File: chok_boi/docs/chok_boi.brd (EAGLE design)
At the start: 372 x 192 mm, 91 parts, among them U1 MPU-6000, U2 DRV8835

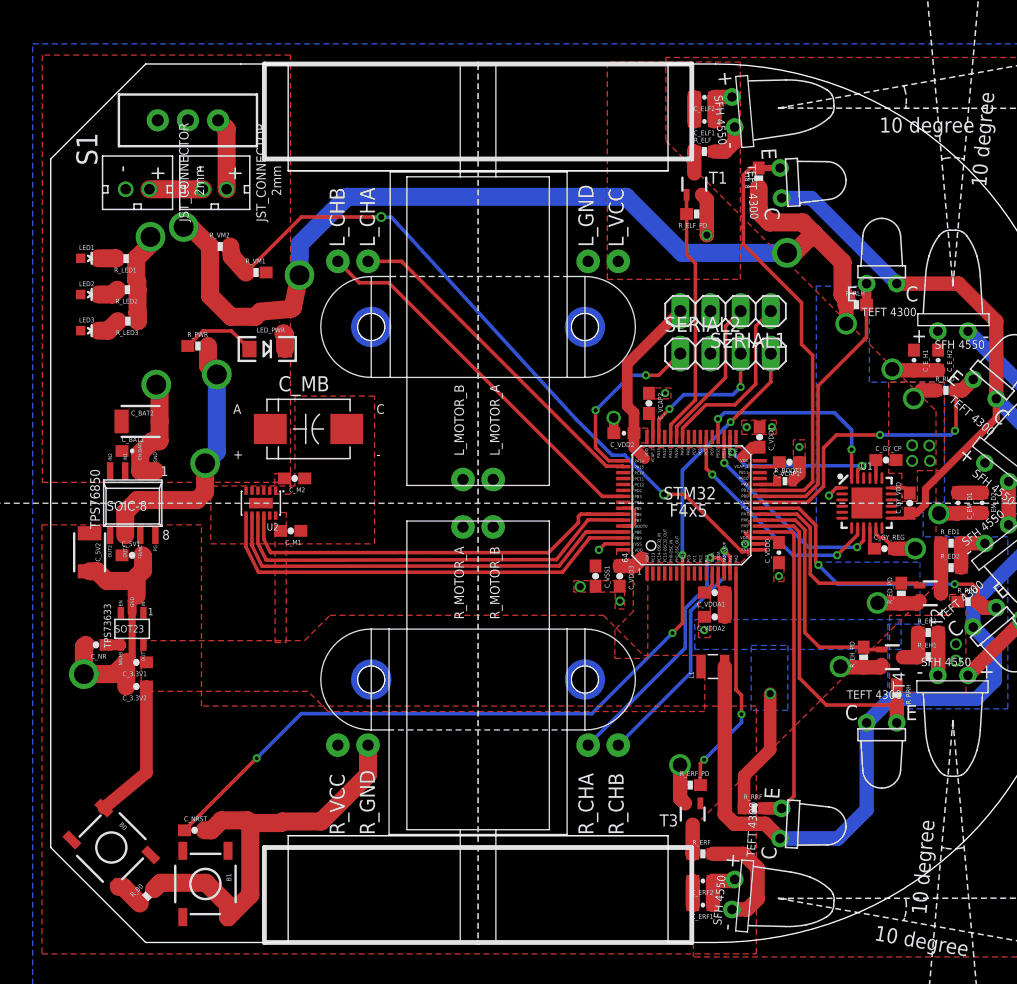
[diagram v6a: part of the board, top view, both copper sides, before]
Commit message: No more airwires!
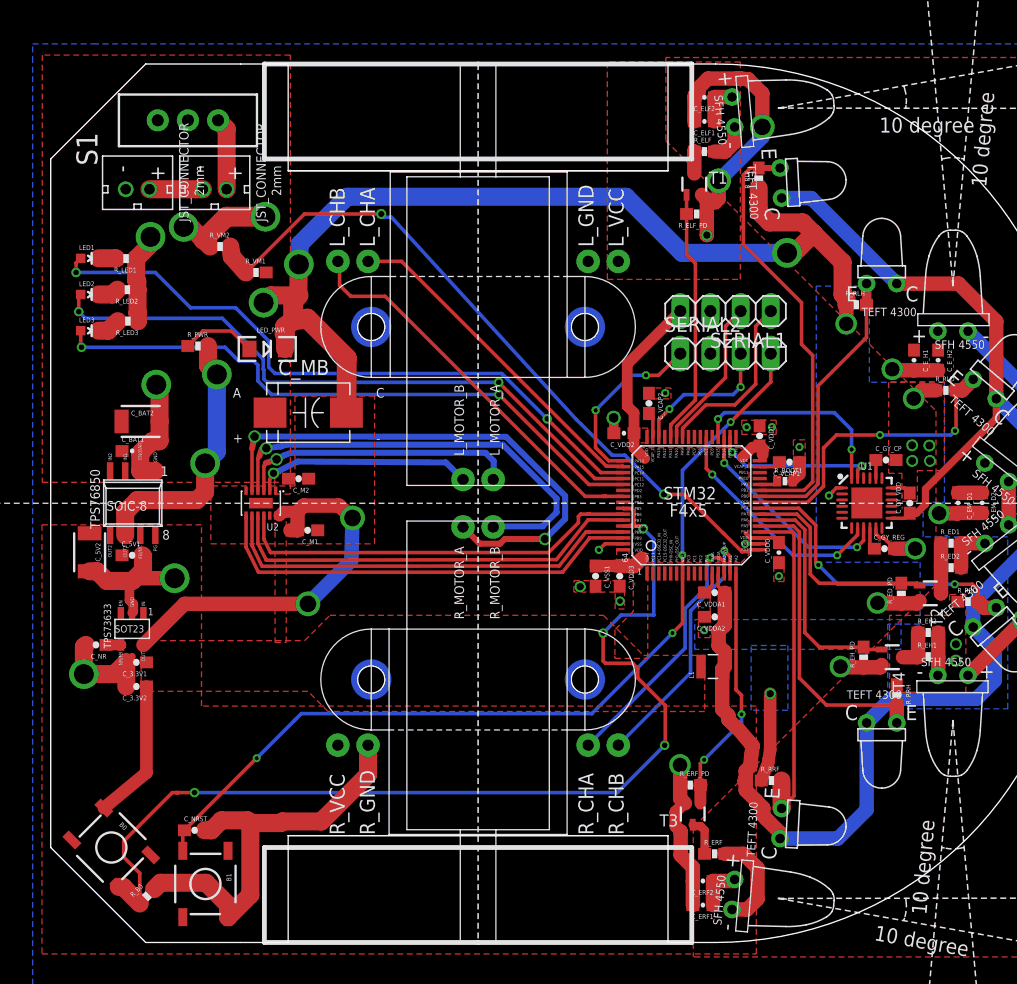
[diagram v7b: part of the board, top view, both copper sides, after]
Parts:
- moved R_RRF 2.75 mm to (60.7, 13.6)
- moved C_M1 1.42 mm to (21.6, 34.7)
- moved C_MB 1.37 mm to (21.7, 44.6)
- moved U$15 1.33 mm to (20.9, 54.5)
- moved U$16 1.15 mm to (20.4, 52.4)
- moved R_ERF 0.99 mm to (55.9, 7.47)
- moved C_M2 0.33 mm to (20.9, 39.1)
- moved C_VDD1 0.10 mm to (59.7, 42.7)
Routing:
- net BOOT0: track 5.49 -> 87.1 mm, vias 0 -> 4
- net LED1: track 0.00 -> 55.7 mm, vias 0 -> 2
- net LED2: track 0.00 -> 54.2 mm, vias 0 -> 2
- net LED3: track 0.00 -> 52.6 mm, vias 0 -> 2
- net MRF: track 0.00 -> 44.9 mm, vias 0 -> 2
- net MRB: track 0.00 -> 37.3 mm, vias 0 -> 1
- net 3.3V: track 33.9 -> 70.5 mm, vias 0 -> 2
- net GND: track 123.9 -> 151.3 mm, vias 20 -> 25
- net MLF: track 0.00 -> 23.6 mm, vias 0 -> 1
- net MLB: track 0.00 -> 18.3 mm, vias 0 -> 1
- net MGND: track 0.00 -> 10.5 mm
- net AGND: track 91.4 -> 86.9 mm
- net A3.3V: track 121.3 -> 125.0 mm
- net RESET: track 75.1 -> 76.9 mm
- net EM_RF: track 19.5 -> 21.0 mm
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
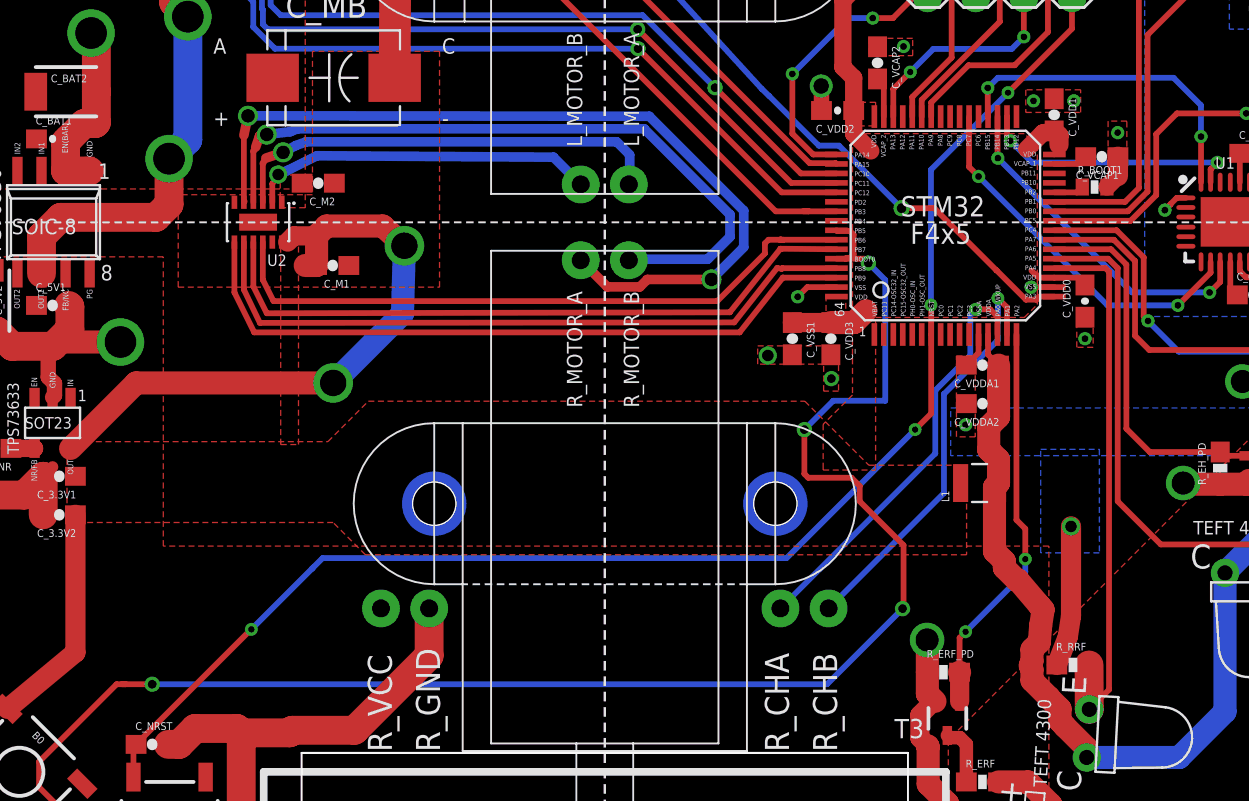
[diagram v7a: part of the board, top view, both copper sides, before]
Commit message: Move Vias further back from MCU
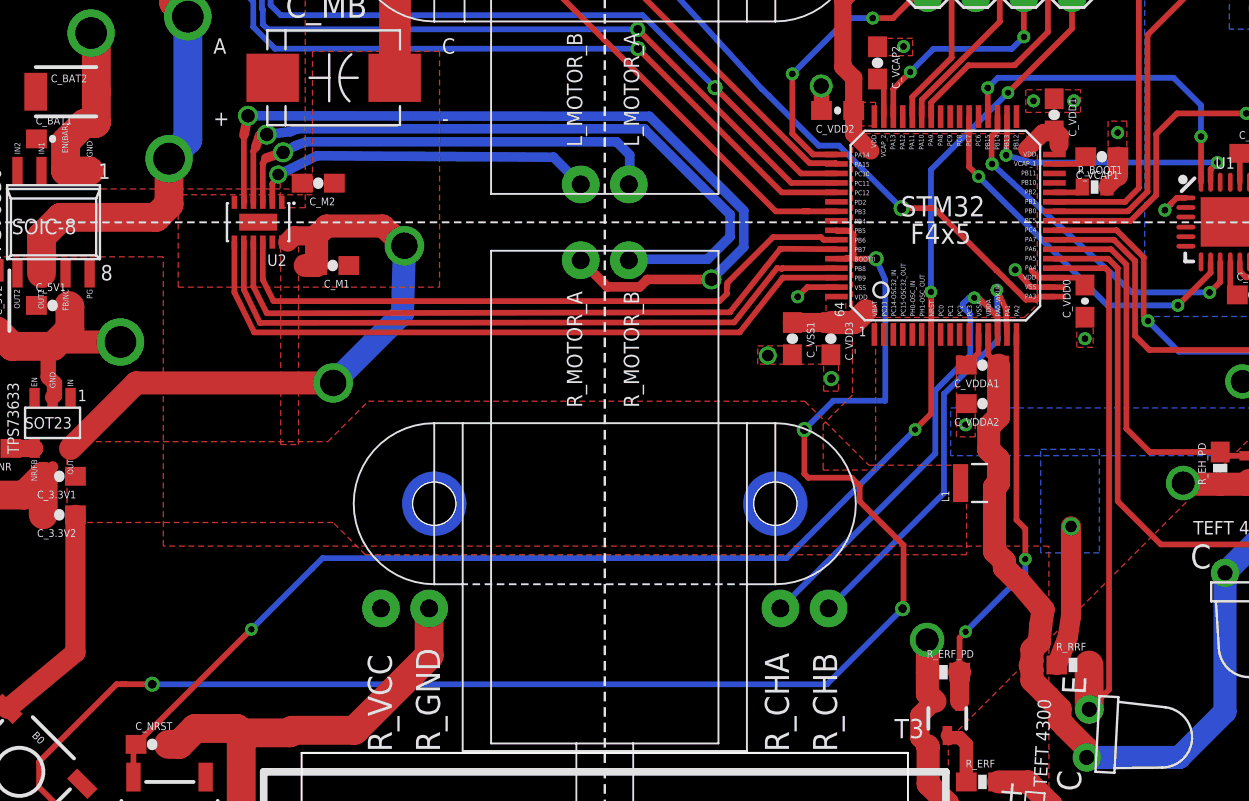
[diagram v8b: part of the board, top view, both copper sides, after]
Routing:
- net ENC_RA: track 22.3 -> 23.7 mm
- net GND: track 151.3 -> 152.5 mm
- net ENC_RB: track 22.2 -> 23.0 mm
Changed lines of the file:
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@@
 <wire x1="63.08" y1="39.443" x2="63.08" y2="40.4622" width="1.0668" layer="1"/>
 <wire x1="58.4974" y1="33.58" x2="59.725" y2="33.58" width="0.3048" layer="1"/>
-<wire x1="58.4974" y1="33.58" x2="58.4962" y2="33.5788" width="0.3048" layer="1"/>
-<via x="58.4962" y="33.5788" extent="1-16" drill="0.3556"/>
+<wire x1="58.4974" y1="33.58" x2="57.658" y2="34.4932" width="0.3048" layer="1"/>
+<via x="57.658" y="34.4932" extent="1-16" drill="0.3556"/>
 <polygon width="0.1524" layer="1" thermals="no">
 <vertex x="60.9092" y="32.4358"/>
@@
 <contactref element="U$5" pad="PB6"/>
 <wire x1="17.9538" y1="35.9578" x2="17.9538" y2="33.970984375" width="0.3048" layer="1"/>
-<wire x1="17.9538" y1="33.970984375" x2="18.5166" y2="32.8422" width="0.3048" layer="1"/>
-<wire x1="18.5166" y1="32.8422" x2="41.9354" y2="32.8422" width="0.3048" layer="1"/>
-<wire x1="44.45" y1="35.3568" x2="44.45" y2="35.8902" width="0.3048" layer="1"/>
-<wire x1="44.45" y1="35.8902" x2="44.6398" y2="36.08" width="0.3048" layer="1"/>
-<wire x1="41.9354" y1="32.8422" x2="44.45" y2="35.3568" width="0.3048" layer="1"/>
-<wire x1="44.6398" y1="36.08" x2="45.227328125" y2="36.08" width="0.3048" layer="1"/>
-<wire x1="45.227328125" y1="36.08" x2="45.279209375" y2="36.10015" width="0.3048" layer="1"/>
-<wire x1="45.279209375" y1="36.10015" x2="45.32495" y2="36.08" width="0.3048" layer="1"/>
-<wire x1="45.32495" y1="36.08" x2="45.39503125" y2="36.08" width="0.3048" layer="1"/>
-<wire x1="45.39503125" y1="36.08" x2="45.4046375" y2="36.08109375" width="0.3048" layer="1"/>
-<wire x1="45.4046375" y1="36.08109375" x2="45.4060125" y2="36.08" width="0.3048" layer="1"/>
-<wire x1="45.4060125" y1="36.08" x2="48.225" y2="36.08" width="0.3048" layer="1"/>
+<wire x1="18.5166" y1="32.8422" x2="17.9538" y2="33.970984375" width="0.3048" layer="1"/>
+<wire x1="47.40355" y1="36.2204" x2="44.8818" y2="36.2204" width="0.3048" layer="1"/>
+<wire x1="48.225" y1="36.08" x2="47.54395" y2="36.08" width="0.3048" layer="1"/>
+<wire x1="47.54395" y1="36.08" x2="47.40355" y2="36.2204" width="0.3048" layer="1"/>
+<wire x1="44.8818" y1="36.2204" x2="42.4688" y2="33.8074" width="0.3048" layer="1"/>
+<wire x1="42.4688" y1="33.8074" x2="42.4688" y2="33.638" width="0.3048" layer="1"/>
+<wire x1="42.4688" y1="33.638" x2="42.4434" y2="33.6126" width="0.3048" layer="1"/>
+<wire x1="42.4434" y1="33.6126" x2="42.4434" y2="33.2232" width="0.3048" layer="1"/>
+<wire x1="42.4434" y1="33.2232" x2="42.0624" y2="32.8422" width="0.3048" layer="1"/>
+<wire x1="42.0624" y1="32.8422" x2="18.5166" y2="32.8422" width="0.3048" layer="1"/>
 </signal>
 <signal name="PWMLF">
@@
 <via x="57.277" y="43.8404" extent="1-16" drill="0.3302"/>
 <wire x1="57.277" y1="43.8404" x2="53.213" y2="39.7764" width="0.3048" layer="16"/>
-<wire x1="53.213" y1="39.7764" x2="53.213" y2="32.639" width="0.3048" layer="16"/>
-<via x="53.213" y="32.639" extent="1-16" drill="0.3302"/>
-<wire x1="53.213" y1="32.639" x2="53.225" y2="32.627" width="0.3048" layer="1"/>
+<wire x1="53.213" y1="39.7764" x2="53.213" y2="33.3248" width="0.3048" layer="16"/>
+<via x="53.213" y="33.3248" extent="1-16" drill="0.3302"/>
+<wire x1="53.213" y1="33.3248" x2="53.225" y2="32.627" width="0.3048" layer="1"/>
 <wire x1="53.225" y1="31.08" x2="53.225" y2="32.627" width="0.3048" layer="1"/>
 <wire x1="11.2658" y1="9.4488" x2="17.3364" y2="15.5194" width="0.3048" layer="1"/>
@@
 <wire x1="17.3482" y1="15.5194" x2="20.5359" y2="18.7071" width="0.3048" layer="16"/>
 <wire x1="20.5359" y1="18.7071" x2="20.6248" y2="18.796" width="0.3048" layer="16"/>
-<wire x1="20.5359" y1="18.7071" x2="21.1074" y2="19.2786" width="0.3048" layer="16"/>
+<wire x1="20.6248" y1="18.796" x2="21.1074" y2="19.2786" width="0.3048" layer="16"/>
 <wire x1="21.1074" y1="19.2786" x2="45.593" y2="19.2786" width="0.3048" layer="16"/>
 <wire x1="45.593" y1="19.2786" x2="52.3748" y2="26.0604" width="0.3048" layer="16"/>
@@
 <wire x1="48.0568" y1="27.5844" x2="50.8" y2="27.5844" width="0.3048" layer="16"/>
 <wire x1="50.8" y1="27.5844" x2="50.8" y2="33.9598" width="0.3048" layer="16"/>
-<wire x1="50.8" y1="33.9598" x2="49.911" y2="34.8488" width="0.3048" layer="16"/>
-<via x="49.911" y="34.8488" extent="1-16" drill="0.4572"/>
-<wire x1="49.911" y1="34.8488" x2="49.6798" y2="35.08" width="0.3048" layer="1"/>
+<wire x1="50.8" y1="33.9598" x2="50.3174" y2="35.0774" width="0.3048" layer="16"/>
+<via x="50.3174" y="35.0774" extent="1-16" drill="0.4572"/>
+<wire x1="50.3174" y1="35.0774" x2="49.6798" y2="35.08" width="0.3048" layer="1"/>
 <wire x1="48.7172" y1="35.08" x2="49.6798" y2="35.08" width="0.3048" layer="1"/>
 <wire x1="48.7172" y1="35.08" x2="48.225" y2="35.08" width="0.3048" layer="1"/>
@@
 <wire x1="6.1468" y1="7.1882" x2="6.1468" y2="8.5344" width="0.3048" layer="1"/>
 <wire x1="6.1468" y1="8.5344" x2="10.2362" y2="12.6238" width="0.3048" layer="1"/>
-<wire x1="10.2362" y1="12.6238" x2="10.7188" y2="12.6238" width="0.3048" layer="1"/>
+<wire x1="10.2362" y1="12.6238" x2="10.5156" y2="12.6238" width="0.3048" layer="1"/>
 </signal>
 <signal name="A3.3V">
@@
 <wire x1="53.4416" y1="28.12938125" x2="55.290009375" y2="29.977790625" width="0.3048" layer="16"/>
 <wire x1="55.290009375" y1="29.977790625" x2="55.290009375" y2="32.125209375" width="0.3048" layer="16"/>
-<wire x1="55.290009375" y1="32.125209375" x2="55.5752" y2="32.4104" width="0.3048" layer="16"/>
-<via x="55.5752" y="32.4104" extent="1-16" drill="0.3302"/>
-<wire x1="55.5752" y1="32.4104" x2="56.3372" y2="32.4104" width="0.3048" layer="1"/>
-<wire x1="56.725" y1="32.0226" x2="56.725" y2="31.08" width="0.3048" layer="1"/>
-<wire x1="56.3372" y1="32.4104" x2="56.725" y2="32.0226" width="0.3048" layer="1"/>
+<via x="55.499" y="33.02" extent="1-16" drill="0.3302"/>
+<wire x1="56.725" y1="31.08" x2="56.725" y2="32.0226" width="0.3048" layer="1"/>
+<wire x1="55.7276" y1="33.02" x2="55.499" y2="33.02" width="0.3048" layer="1"/>
+<wire x1="56.725" y1="32.0226" x2="55.7276" y2="33.02" width="0.3048" layer="1"/>
+<wire x1="55.290009375" y1="32.125209375" x2="54.8894" y2="32.52581875" width="0.3048" layer="16"/>
+<wire x1="54.8894" y1="32.52581875" x2="54.8894" y2="32.6898" width="0.3048" layer="16"/>
+<wire x1="54.8894" y1="32.6898" x2="55.2196" y2="33.02" width="0.3048" layer="16"/>
+<wire x1="55.2196" y1="33.02" x2="55.499" y2="33.02" width="0.3048" layer="16"/>
 </signal>
 <signal name="ENC_RB">
@@
 <wire x1="53.8988" y1="22.7138" x2="53.8988" y2="27.94" width="0.3048" layer="16"/>
 <wire x1="53.8988" y1="27.94" x2="56.7436" y2="30.7848" width="0.3048" layer="16"/>
-<wire x1="56.7436" y1="30.7848" x2="56.7436" y2="32.9946" width="0.3048" layer="16"/>
-<via x="56.7436" y="32.9946" extent="1-16" drill="0.3302"/>
-<wire x1="56.7436" y1="32.9946" x2="57.225" y2="32.5132" width="0.3048" layer="1"/>
-<wire x1="57.225" y1="32.5132" x2="57.225" y2="31.08" width="0.3048" layer="1"/>
+<wire x1="56.7436" y1="30.7848" x2="56.6928" y2="33.4264" width="0.3048" layer="16"/>
+<via x="56.6928" y="33.4264" extent="1-16" drill="0.3302"/>
+<wire x1="56.6928" y1="33.4264" x2="57.1742" y2="32.4116" width="0.3048" layer="1"/>
+<wire x1="57.1742" y1="32.4116" x2="57.225" y2="31.08" width="0.3048" layer="1"/>
 </signal>
 <signal name="LED1">
@@
 <contactref element="U$5" pad="PB13"/>
 <wire x1="57.2262" y1="42.5788" x2="57.225" y2="42.58" width="0.3048" layer="1"/>
-<via x="57.404" y="41.3004" extent="1-16" drill="0.35"/>
-<wire x1="57.404" y1="41.3004" x2="57.2262" y2="41.4782" width="0.3048" layer="1"/>
+<via x="57.1754" y="40.5384" extent="1-16" drill="0.35"/>
+<wire x1="57.1754" y1="40.5384" x2="57.2262" y2="41.4782" width="0.3048" layer="1"/>
 <wire x1="57.2262" y1="41.4782" x2="57.2262" y2="42.5788" width="0.3048" layer="1"/>
 <wire x1="67.9703" y1="39.1148" x2="67.9703" y2="39.8005" width="0.3048" layer="1"/>
@@
 <via x="68.326" y="40.1562" extent="1-16" drill="0.3556"/>
 <wire x1="68.326" y1="40.1562" x2="58.5482" y2="40.1562" width="0.3048" layer="16"/>
-<wire x1="58.5482" y1="40.1562" x2="57.404" y2="41.3004" width="0.3048" layer="16"/>
+<wire x1="58.5482" y1="40.1562" x2="57.1754" y2="40.5384" width="0.3048" layer="16"/>
 </signal>
 <signal name="MISO">
 <contactref element="U1" pad="9"/>
 <contactref element="U$5" pad="PB14"/>
-<wire x1="56.725" y1="42.58" x2="56.725" y2="40.4046" width="0.3048" layer="1"/>
-<wire x1="56.725" y1="40.4046" x2="56.7436" y2="40.386" width="0.3048" layer="1"/>
-<via x="56.7436" y="40.386" extent="1-16" drill="0.35"/>
-<wire x1="56.7436" y1="40.386" x2="63.8302" y2="33.2994" width="0.3048" layer="16"/>
+<via x="56.4388" y="40.0812" extent="1-16" drill="0.35"/>
+<wire x1="56.4388" y1="40.0812" x2="63.8302" y2="33.2994" width="0.3048" layer="16"/>
 <wire x1="63.8302" y1="33.2994" x2="67.9196" y2="33.2994" width="0.3048" layer="16"/>
 <via x="67.9196" y="33.2994" extent="1-16" drill="0.35"/>
 <wire x1="67.9196" y1="33.2994" x2="68.4749" y2="33.8547" width="0.3048" layer="1"/>
 <wire x1="68.4749" y1="33.8547" x2="68.4749" y2="34.9116" width="0.3048" layer="1"/>
+<wire x1="56.725" y1="42.58" x2="56.725" y2="41.8406" width="0.3048" layer="1"/>
+<wire x1="56.725" y1="41.8406" x2="56.4134" y2="41.529" width="0.3048" layer="1"/>
+<wire x1="56.4134" y1="41.529" x2="56.4134" y2="40.1066" width="0.3048" layer="1"/>
+<wire x1="56.4134" y1="40.1066" x2="56.4388" y2="40.0812" width="0.3048" layer="1"/>
 </signal>
 <signal name="MOSI">
